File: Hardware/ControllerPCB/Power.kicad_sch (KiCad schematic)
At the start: 44 parts, among them Q1 NMOS_SO-8, U2 BTN9960LV, U3 BTN9960LV, U4 INA180A2, U6 TSR 0.5-2433

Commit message: Update PCB
Add solder jumper for +3.3V selection
fix DRC
aligne vias
export Gerber
add text
fix 3D Models
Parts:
- added JP6: SolderJumper_2_Open, Jumper:SolderJumper-2_P1.3mm_Open_TrianglePad1.0x1.5mm, symbol Jumper:SolderJumper_2_Open
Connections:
- net +3.3V: now also JP6.2 (B); no longer U6.3 (+VOUT)
- new net 3V3: JP6.1 (A), U6.3 (+VOUT)
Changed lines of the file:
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@@
   (junction (at 82.55 64.77) (diameter 0) (color 0 0 0 0)
   )
-  (junction (at 123.19 173.99) (diameter 0) (color 0 0 0 0)
+  (junction (at 129.54 173.99) (diameter 0) (color 0 0 0 0)
   )
   (junction (at 238.76 109.22) (diameter 0) (color 0 0 0 0)
@@
     (stroke (width 0) (type default))
   )
-  (wire (pts (xy 123.19 173.99) (xy 128.27 173.99))
+  (wire (pts (xy 129.54 173.99) (xy 134.62 173.99))
     (stroke (width 0) (type default))
   )
@@
     (stroke (width 0) (type default))
   )
-  (wire (pts (xy 119.38 173.99) (xy 123.19 173.99))
+  (wire (pts (xy 119.38 173.99) (xy 120.65 173.99))
     (stroke (width 0) (type default))
   )
@@
     (stroke (width 0) (type default))
   )
+  (wire (pts (xy 128.27 173.99) (xy 129.54 173.99))
+    (stroke (width 0) (type default))
+  )
   (wire (pts (xy 73.66 68.58) (xy 73.66 64.77))
     (stroke (width 0) (type default))
@@
     (stroke (width 0) (type default))
   )
-  (wire (pts (xy 123.19 170.18) (xy 123.19 173.99))
+  (wire (pts (xy 129.54 170.18) (xy 129.54 173.99))
     (stroke (width 0) (type default))
   )
@@
   (wire (pts (xy 77.47 31.75) (xy 77.47 33.02))
     (stroke (width 0) (type default))
+  )
+  (label "3V3" (at 119.38 173.99 0) (fields_autoplaced)
+    (effects (font (size 1.27 1.27)) (justify left bottom))
   )
   (label "+VBat*" (at 52.07 24.13 0) (fields_autoplaced)
@@
     (effects (font (size 1.27 1.27)) (justify right))
   )
-  (hierarchical_label "+3V3" (shape input) (at 128.27 173.99 0) (fields_autoplaced)
+  (hierarchical_label "+3V3" (shape input) (at 134.62 173.99 0) (fields_autoplaced)
     (effects (font (size 1.27 1.27)) (justify left))
   )
@@
     )
   )
-  (symbol (lib_id "power:+3.3V") (at 123.19 170.18 0) (unit 1)
+  (symbol (lib_id "power:+3.3V") (at 129.54 170.18 0) (unit 1)
     (in_bom yes) (on_board yes) (dnp no) (fields_autoplaced)
-    (property "Reference" "#PWR039" (at 123.19 173.99 0)
-      (effects (font (size 1.27 1.27)) hide)
-    )
-    (property "Value" "+3.3V" (at 123.19 165.1 0)
-      (effects (font (size 1.27 1.27)))
-    )
-    (property "Footprint" "" (at 123.19 170.18 0)
-      (effects (font (size 1.27 1.27)) hide)
-    )
-    (property "Datasheet" "" (at 123.19 170.18 0)
+    (property "Reference" "#PWR039" (at 129.54 173.99 0)
+      (effects (font (size 1.27 1.27)) hide)
+    )
+    (property "Value" "+3.3V" (at 129.54 165.1 0)
+      (effects (font (size 1.27 1.27)))
+    )
+    (property "Footprint" "" (at 129.54 170.18 0)
+      (effects (font (size 1.27 1.27)) hide)
+    )
+    (property "Datasheet" "" (at 129.54 170.18 0)
       (effects (font (size 1.27 1.27)) hide)
     )
@@
         )
       )
+    )
+  )
+  (symbol (lib_id "Jumper:SolderJumper_2_Open") (at 124.46 173.99 0) (unit 1)
+    (in_bom yes) (on_board yes) (dnp no)
+    (property "Reference" "JP6" (at 124.46 167.64 0)
+      (effects (font (size 1.27 1.27)))
+    )
+    (property "Value" "SolderJumper_2_Open" (at 124.46 177.8 0)
+      (effects (font (size 1.27 1.27)))
+    )
+    (property "Footprint" "Jumper:SolderJumper-2_P1.3mm_Open_TrianglePad1.0x1.5mm" (at 124.46 173.99 0)
+      (effects (font (size 1.27 1.27)) hide)
+    )
+    (property "Datasheet" "~" (at 124.46 173.99 0)
+      (effects (font (size 1.27 1.27)) hide)
+    )
+    (pin "1")
+    (pin "2")
+    (instances
+      (project "BugWiperPCB"
+        (path "/d31a15bd-db02-4d4c-9593-17c596d3182c/c3388659-287d-4904-b92a-4db1b844f22c"
+          (reference "JP6") (unit 1)
+        )
+      )

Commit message: update Controller PCB
Add additional capacitor
fix footprint Resistor Array CAT16
fix 3D Model CAT16
change traces from 0.5 to 0.4 mm
fix USB-C Footprint
Export Gerber
update BOM and Values
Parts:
- added C41: 1nF, Capacitor_SMD:C_0805_2012Metric_Pad1.18x1.45mm_HandSolder, symbol Device:C
- Q1: value NMOS_SO-8 -> SQJ146ELP-T1_GE3; Manufacturer_Name (none) -> Vishay; Manufacturer_Part_Number (none) -> SQJ146ELP-T1_GE3; Package (none) -> SO-8; Price (none) -> 1,00€
- U2, U3: Manufacturer_Name (none) -> infineon; Manufacturer_Part_Number (none) -> BTN9960LVAUMA1; Mouser Part Number (none) -> 726-BTN9960LVAUMA1; Price (none) -> 3,50€
- U4: Manufacturer_Name (none) -> texasinstruments; Manufacturer_Part_Number (none) -> INA180A2IDBVT; Mouser Part Number (none) -> 595-INA180A2IDBVT; Price (none) -> 0,85€
- U6: Alternative MF (none) -> RECOM; Alternative PN (none) -> R-78E3.3-0.5; Alternative Price (none) -> 2,5€; Manufacturer_Name (none) -> TRACO Power; Manufacturer_Part_Number (none) -> TSR 0.5-2433; Mouser Part Number (none) -> 495-TSR0.5-2433; Package (none) -> TO-220 compatible SIP3 package; Price (none) -> 6,44€
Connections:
- net 3V3: now also C41.2
- net at C26.2, L2.2, U6.1 (+VIN): now also C41.1
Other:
- moved on the sheet: JP6

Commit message: update BOM
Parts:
- C10, C7: value 100uF -> 22uF 25V; Manufacturer_Name (none) -> Samsung; Manufacturer_Part_Number (none) -> CL31A226KAHNNNE; Mouser Part Number (none) -> 187-CL31A226KAHNNNE; Mouser Price/Stock (none) -> 0,20€
- C11, C12, C13: Manufacturer_Name (none) -> KYOCERA AVX; Manufacturer_Part_Number (none) -> KAM15AR71H102KM; Mouser Part Number (none) -> 581-KAM15AR71H102KM; Mouser Price/Stock (none) -> 0,036€
- C14: value 10nF -> 10nF; Manufacturer_Name (none) -> Samsung; Manufacturer_Part_Number (none) -> CL10B103KB8NFNC; Mouser Part Number (none) -> 187-CL10B103KB8NFNC; Mouser Price/Stock (none) -> 0,016 €
- C15, C16, C17, C21, C23: value 25uF -> 22uF 25V; Manufacturer_Name (none) -> Samsung; Manufacturer_Part_Number (none) -> CL31A226KAHNNNE; Mouser Part Number (none) -> 187-CL31A226KAHNNNE; Mouser Price/Stock (none) -> 0,20€
- C18, C19, C20, C28: value 470uF -> 470uF 16V; Manufacturer_Name (none) -> Nichicon; Manufacturer_Part_Number (none) -> UWT1E331MNL1GS; Mouser Part Number (none) -> 647-UWT1E331MNL1S; Mouser Price/Stock (none) -> 0,256€
- C24, C25, C26: value 4.7uF -> 22uF 25V; Manufacturer_Name (none) -> Samsung; Manufacturer_Part_Number (none) -> CL31A226KAHNNNE; Mouser Part Number (none) -> 187-CL31A226KAHNNNE; Mouser Price/Stock (none) -> 0,20€
- C31: value 100nF -> 100nF; Manufacturer_Name (none) -> Samsung; Manufacturer_Part_Number (none) -> CL10B104KB8NNNC; Mouser Part Number (none) -> 187-CL10B104KB8NNNC; Mouser Price/Stock (none) -> 0,01 €
- C5, C9: value 100nF -> 1uF 50V; footprint Capacitor_SMD:C_0603_1608Metric -> Capacitor_SMD:C_0805_2012Metric; Manufacturer_Name (none) -> Samsung; Manufacturer_Part_Number (none) -> CL21B105MBFNNNE; Mouser Part Number (none) -> 187-CL21B105MBFNNNE; Mouser Price/Stock (none) -> 0,026€
- C6, C8, R7, R8: now left out of the parts list
- D2: value D_Zener -> D_Zener 10V; footprint Resistor_SMD:R_0805_2012Metric -> Diode_SMD:D_SOD-323_HandSoldering; Manufacturer_Name (none) -> Vishay; Manufacturer_Part_Number (none) -> GDZ10B-E3-08; Mouser Part Number (none) -> 78-GDZ10B-E3-08; Mouser Price/Stock (none) -> 0,143 €
- D3: value D_TVS -> D_TVS 15V
- L1: value IHLP4040DZER100M1A -> IHLP4040DZER100M11; Manufacturer_Name (none) -> Vishay; Manufacturer_Part_Number (none) -> IHLP4040DZER100M11; Mouser Part Number (none) -> 70-IHLP4040DZER100M1; Mouser Price/Stock (none) -> 1,18 €
- L2: Manufacturer_Name (none) -> Wurth Elektronik; Manufacturer_Part_Number (none) -> 74477410; Mouser Part Number (none) -> 710-74477410; Mouser Price/Stock (none) -> 1,61€
- Q1: Mouser Part Number (none) -> 78-SQJ146ELP-T1_GE3; Mouser Price/Stock (none) -> 1,02 €
- R10, R11: value 4k7 -> 10k
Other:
- moved on the sheet: C11, C12, C14, C16, C17, C18, C24, C25, C26, C28, C41, D2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

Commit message: update
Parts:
- D2: value D_Zener 10V -> GDZ10B-E3-08
- JP6: now left out of the parts list
- L2: value 10µH 2.2A -> 10uH 2.2A 74477410; JLCPCB Part # (none) -> C324269; JLCPCB Price (none) -> 0.1270; Nr 74477410 -> (none)
- R10, R11, R21, R38: Manufacturer_Name (none) -> YAGEO; Manufacturer_Part_Number (none) -> RC0603FR-1010KL; Mouser Part Number (none) -> 603-RC0603FR-1010KL; Mouser Price/Stock (none) -> 0,008 €
- R12, R9: Manufacturer_Name (none) -> YAGEO; Manufacturer_Part_Number (none) -> RC0603FR-071KL; Mouser Part Number (none) -> 603-RC0603FR-071KL; Mouser Price/Stock (none) -> 0,009 €
- R19: Manufacturer_Name (none) -> Bourns; Manufacturer_Part_Number (none) -> CR0603-FX-3301ELF; Mouser Part Number (none) -> 652-CR0603-FX3301ELF; Mouser Price/Stock (none) -> 0,009 €
- R20: Manufacturer_Name (none) -> YAGEO; Manufacturer_Part_Number (none) -> AC0603FR-1022KL; Mouser Part Number (none) -> 603-AC0603FR-1022KL; Mouser Price/Stock (none) -> 0,01 €
- R25: Manufacturer_Name (none) -> Welwyn Components / TT Electronics; Manufacturer_Part_Number (none) -> LRMAM1206-R004FT5; Mouser Part Number (none) -> 756-LRMAM1206R004FT5; Mouser Price/Stock (none) -> 0,57 €
- TH1: value Thermistor_NTC -> 10k NTC; Manufacturer_Name (none) -> Murata; Manufacturer_Part_Number (none) -> NCU18XH103E60RB; Mouser Part Number (none) -> 81-NCU18XH103E60RB; Mouser Price/Stock (none) -> 0,095 €
- U2, U3: Mouser Price/Stock (none) -> 2,40 €
- U4: JLCPCB Part # (none) -> C116203; JLCPCB Price (none) -> 0.2074; Mouser Price/Stock (none) -> 0,855€
- U6: Alternative MF RECOM -> TRACO Power; Alternative PN R-78E3.3-0.5 -> TSR 0.5-2433; Alternative Price 2,5€ -> 6,44 €; Manufacturer_Name TRACO Power -> RECOM; Manufacturer_Part_Number TSR 0.5-2433 -> R-78E3.3-0.5; Mouser Part Number 495-TSR0.5-2433 -> 919-R-78E3.3-0.5; Mouser Price/Stock (none) -> 2,75€; Package TO-220 compatible SIP3 package -> (none)

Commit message: update PCB and Gerber
change Switches to cheaper ones
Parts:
- C18, C19, C20, C28: value 470uF 16V -> 330uF 25V
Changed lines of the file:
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@@
       (effects (font (size 1.27 1.27)) (justify left))
     )
-    (property "Value" "470uF 16V" (at 66.04 74.93 0)
+    (property "Value" "330uF 25V" (at 66.04 74.93 0)
       (effects (font (size 1.27 1.27)) (justify left))
     )
@@
       (effects (font (size 1.27 1.27)) (justify left))
     )
-    (property "Value" "470uF 16V" (at 107.95 43.18 90)
+    (property "Value" "330uF 25V" (at 107.95 43.18 90)
       (effects (font (size 1.27 1.27)) (justify left))
     )
@@
       (effects (font (size 1.27 1.27)) (justify left))
     )
-    (property "Value" "470uF 16V" (at 74.93 74.93 0)
+    (property "Value" "330uF 25V" (at 74.93 74.93 0)
       (effects (font (size 1.27 1.27)) (justify left))
     )
@@
       (effects (font (size 1.27 1.27)) (justify left))
     )
-    (property "Value" "470uF 16V" (at 116.84 43.18 90)
-      (effects (font (size 1.27 1.27)) (justify left))
-    )
+    (property "Value" "330uF 25V" (at 116.84 43.18 90)
+      (effects (font (size 1.27 1.27)) (justify left))
+    )

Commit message: update BOM
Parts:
- C41: now left out of the parts list
- D3: value D_TVS 15V -> D_TVS 14V; Manufacturer_Name (none) -> Diodes Incorporated; Manufacturer_Part_Number (none) -> SMBJ14CA-13-F; Mouser Part Number (none) -> 621-SMBJ14CA-13-F; Mouser Price/Stock (none) -> 0,219 €
- Q1: Price 1,00€ -> (none)
- R7, R8: value 47k -> 22k; Manufacturer_Name (none) -> YAGEO; Manufacturer_Part_Number (none) -> AC0603FR-1022KL; Mouser Part Number (none) -> 603-AC0603FR-1022KL; Mouser Price/Stock (none) -> 0,01 €; now fitted; now in the parts list
- U2, U3: Price 3,50€ -> (none)
- U4: Price 0,85€ -> (none)
- U6: Price 6,44€ -> (none)
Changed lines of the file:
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@@
-      (effects (font (size 1.27 1.27)) hide)
-    )
-    (property "Price" "0,85€" (at 49.53 77.47 0)
       (effects (font (size 1.27 1.27)) hide)
     )
@@
     )
     (property "Mouser Part Number" "726-BTN9960LVAUMA1" (at 213.36 88.9 0)
-      (effects (font (size 1.27 1.27)) hide)
-    )
-    (property "Price" "3,50€" (at 213.36 88.9 0)
       (effects (font (size 1.27 1.27)) hide)
     )
@@
   )
   (symbol (lib_id "Device:R") (at 242.57 55.88 0) (unit 1)
-    (in_bom no) (on_board yes) (dnp yes) (fields_autoplaced)
+    (in_bom yes) (on_board yes) (dnp no) (fields_autoplaced)
     (property "Reference" "R7" (at 245.11 54.61 0)
       (effects (font (size 1.27 1.27)) (justify left))
     )
-    (property "Value" "47k" (at 245.11 57.15 0)
+    (property "Value" "22k" (at 245.11 57.15 0)
       (effects (font (size 1.27 1.27)) (justify left))
     )
@@
     )
     (property "JLCPCB Price" "" (at 242.57 55.88 0)
+      (effects (font (size 1.27 1.27)) hide)
+    )
+    (property "Manufacturer_Name" "YAGEO" (at 242.57 55.88 0)
+      (effects (font (size 1.27 1.27)) hide)
+    )
+    (property "Manufacturer_Part_Number" "AC0603FR-1022KL" (at 242.57 55.88 0)
+      (effects (font (size 1.27 1.27)) hide)
+    )
+    (property "Mouser Part Number" "603-AC0603FR-1022KL" (at 242.57 55.88 0)
+      (effects (font (size 1.27 1.27)) hide)
+    )
+    (property "Mouser Price/Stock" "0,01 €" (at 242.57 55.88 0)
       (effects (font (size 1.27 1.27)) hide)
     )
@@
       (effects (font (size 1.27 1.27)) (justify right))
     )
-    (property "Value" "D_TVS 15V" (at 62.23 27.94 0)
+    (property "Value" "D_TVS 14V" (at 62.23 27.94 0)
       (effects (font (size 1.27 1.27)) (justify right))
     )
@@
       (effects (font (size 1.27 1.27)) hide)
     )
+    (property "Manufacturer_Name" "Diodes Incorporated" (at 59.69 31.75 0)
+      (effects (font (size 1.27 1.27)) hide)
+    )
+    (property "Manufacturer_Part_Number" "SMBJ14CA-13-F" (at 59.69 31.75 0)
+      (effects (font (size 1.27 1.27)) hide)
+    )
+    (property "Mouser Part Number" "621-SMBJ14CA-13-F" (at 59.69 31.75 0)
+      (effects (font (size 1.27 1.27)) hide)
+    )
+    (property "Mouser Price/Stock" "0,219 €" (at 59.69 31.75 0)
+      (effects (font (size 1.27 1.27)) hide)
+    )
     (pin "2")
     (pin "1")
@@
   )
   (symbol (lib_id "Device:R") (at 242.57 105.41 0) (unit 1)
-    (in_bom no) (on_board yes) (dnp yes) (fields_autoplaced)
+    (in_bom yes) (on_board yes) (dnp no) (fields_autoplaced)
     (property "Reference" "R8" (at 245.11 104.14 0)
       (effects (font (size 1.27 1.27)) (justify left))
     )
-    (property "Value" "47k" (at 245.11 106.68 0)
+    (property "Value" "22k" (at 245.11 106.68 0)
       (effects (font (size 1.27 1.27)) (justify left))
     )
@@
     )
     (property "JLCPCB Price" "" (at 242.57 105.41 0)
+      (effects (font (size 1.27 1.27)) hide)
+    )
+    (property "Manufacturer_Name" "YAGEO" (at 242.57 105.41 0)
+      (effects (font (size 1.27 1.27)) hide)
+    )
+    (property "Manufacturer_Part_Number" "AC0603FR-1022KL" (at 242.57 105.41 0)
+      (effects (font (size 1.27 1.27)) hide)
+    )
+    (property "Mouser Part Number" "603-AC0603FR-1022KL" (at 242.57 105.41 0)
+      (effects (font (size 1.27 1.27)) hide)
+    )
+    (property "Mouser Price/Stock" "0,01 €" (at 242.57 105.41 0)
       (effects (font (size 1.27 1.27)) hide)
     )
@@
   )
   (symbol (lib_id "Device:C") (at 92.71 133.35 90) (unit 1)
-    (in_bom yes) (on_board yes) (dnp yes)
+    (in_bom no) (on_board yes) (dnp yes)
     (property "Reference" "C41" (at 93.98 127 90)
       (effects (font (size 1.27 1.27)) (justify left))
@@
     )
     (property "Mouser Part Number" "726-BTN9960LVAUMA1" (at 213.36 39.37 0)
-      (effects (font (size 1.27 1.27)) hide)
-    )
-    (property "Price" "3,50€" (at 213.36 39.37 0)
       (effects (font (size 1.27 1.27)) hide)
     )
@@
       (effects (font (size 1.27 1.27)) hide)
     )
-    (property "Price" "6,44€" (at 72.39 147.32 0)
-      (effects (font (size 1.27 1.27)) hide)
-    )
     (property "Mouser Price/Stock" "2,75€" (at 72.39 147.32 0)
       (effects (font (size 1.27 1.27)) hide)
@@
       (effects (font (size 1.27 1.27)) hide)
     )
-    (property "Price" "1,00€" (at 68.58 26.67 0)
-      (effects (font (size 1.27 1.27)) hide)
-    )
     (property "Alternative MF" "" (at 68.58 26.67 0)
       (effects (font (size 1.27 1.27)) hide)
@@
       (effects (font (size 1.27 1.27)) hide)
     )
-    (property "Nr" "" (at 62.23 147.32 0)
-      (effects (font (size 1.27 1.27)) hide)
-    )

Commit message: update PCB to view Values and Refs
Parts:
- C10, C15, C16, C17, C21, C23, C24, C25, C26, C7: value 22uF 25V -> 22uF
- C14: value 10nF -> 10nF
- C18, C19, C20, C28: value 330uF 25V -> 330uF
- C31: value 100nF -> 100nF
- C5, C9: value 1uF 50V -> 1uF
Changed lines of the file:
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@@
       (effects (font (size 1.27 1.27)) (justify left))
     )
-    (property "Value" "22uF 25V" (at 90.17 41.91 90)
+    (property "Value" "22uF" (at 90.17 41.91 90)
       (effects (font (size 1.27 1.27)) (justify left))
     )
@@
       (effects (font (size 1.27 1.27)) (justify left))
     )
-    (property "Value" "22uF 25V" (at 45.72 151.13 90)
+    (property "Value" "22uF" (at 45.72 151.13 90)
       (effects (font (size 1.27 1.27)) (justify left))
     )
@@
       (effects (font (size 1.27 1.27)) (justify left))
     )
-    (property "Value" "22uF 25V" (at 68.58 151.13 90)
+    (property "Value" "22uF" (at 68.58 151.13 90)
       (effects (font (size 1.27 1.27)) (justify left))
     )
@@
       (effects (font (size 1.27 1.27)) (justify left))
     )
-    (property "Value" "22uF 25V" (at 33.02 151.13 90)
+    (property "Value" "22uF" (at 33.02 151.13 90)
       (effects (font (size 1.27 1.27)) (justify left))
     )
@@
       (effects (font (size 1.27 1.27)) (justify left))
     )
-    (property "Value" "22uF 25V" (at 54.61 27.94 90)
+    (property "Value" "22uF" (at 54.61 27.94 90)
       (effects (font (size 1.27 1.27)) (justify left))
     )
@@
       (effects (font (size 1.27 1.27)) (justify left))
     )
-    (property "Value" "330uF 25V" (at 66.04 74.93 0)
+    (property "Value" "330uF" (at 66.04 74.93 0)
       (effects (font (size 1.27 1.27)) (justify left))
     )
@@
       (effects (font (size 1.27 1.27)) (justify left))
     )
-    (property "Value" "1uF 50V" (at 255.27 57.15 0)
+    (property "Value" "1uF" (at 255.27 57.15 0)
       (effects (font (size 1.27 1.27)) (justify left))
     )
@@
       (effects (font (size 1.27 1.27)) (justify left))
     )
-    (property "Value" "22uF 25V" (at 269.24 106.68 0)
+    (property "Value" "22uF" (at 269.24 106.68 0)
       (effects (font (size 1.27 1.27)) (justify left))
     )
@@
       (effects (font (size 1.27 1.27)) (justify left))
     )
-    (property "Value" "330uF 25V" (at 107.95 43.18 90)
+    (property "Value" "330uF" (at 107.95 43.18 90)
       (effects (font (size 1.27 1.27)) (justify left))
     )
@@
       (effects (font (size 1.27 1.27)) (justify left))
     )
-    (property "Value" "22uF 25V" (at 33.02 35.56 90)
+    (property "Value" "22uF" (at 33.02 35.56 90)
       (effects (font (size 1.27 1.27)) (justify left))
     )
@@
       (effects (font (size 1.27 1.27)) (justify left))
     )
-    (property "Value" "330uF 25V" (at 74.93 74.93 0)
+    (property "Value" "330uF" (at 74.93 74.93 0)
       (effects (font (size 1.27 1.27)) (justify left))
     )
@@
       (effects (font (size 1.27 1.27)) (justify left))
     )
-    (property "Value" "22uF 25V" (at 83.82 74.93 0)
+    (property "Value" "22uF" (at 83.82 74.93 0)
       (effects (font (size 1.27 1.27)) (justify left))
     )
@@
       (effects (font (size 1.27 1.27)) (justify left))
     )
-    (property "Value" "330uF 25V" (at 116.84 43.18 90)
+    (property "Value" "330uF" (at 116.84 43.18 90)
       (effects (font (size 1.27 1.27)) (justify left))
     )
@@
       (effects (font (size 1.27 1.27)) (justify left))
     )
-    (property "Value" "22uF 25V" (at 99.06 41.91 90)
+    (property "Value" "22uF" (at 99.06 41.91 90)
       (effects (font (size 1.27 1.27)) (justify left))
     )
@@
       (effects (font (size 1.27 1.27)) (justify left))
     )
-    (property "Value" "100nF " (at 212.09 144.78 0)
+    (property "Value" "100nF" (at 212.09 144.78 0)
       (effects (font (size 1.27 1.27)) (justify left))
     )
@@
       (effects (font (size 1.27 1.27)) (justify left))
     )
-    (property "Value" "22uF 25V" (at 269.24 57.15 0)
+    (property "Value" "22uF" (at 269.24 57.15 0)
       (effects (font (size 1.27 1.27)) (justify left))
     )
@@
       (effects (font (size 1.27 1.27)) (justify left))
     )
-    (property "Value" "1uF 50V" (at 255.27 106.68 0)
+    (property "Value" "1uF" (at 255.27 106.68 0)
       (effects (font (size 1.27 1.27)) (justify left))
     )
@@
       (effects (font (size 1.27 1.27)) (justify left))
     )
-    (property "Value" "10nF " (at 72.39 43.18 0)
-      (effects (font (size 1.27 1.27)) (justify left))
-    )
+    (property "Value" "10nF" (at 72.39 43.18 0)
+      (effects (font (size 1.27 1.27)) (justify left))
+    )

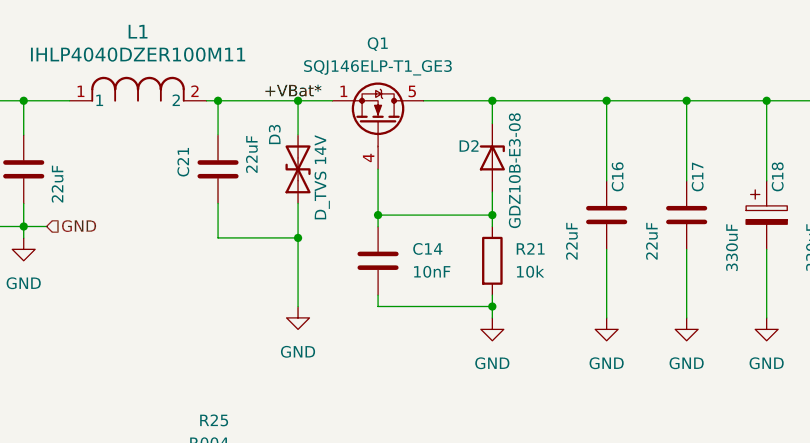
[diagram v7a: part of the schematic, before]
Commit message: update Controller PCB PDF Export and layer of Values and Reference
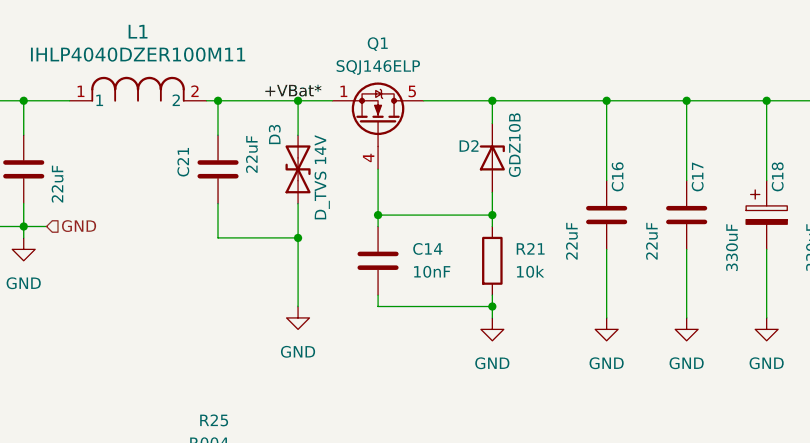
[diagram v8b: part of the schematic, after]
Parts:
- D2: value GDZ10B-E3-08 -> GDZ10B
- Q1: value SQJ146ELP-T1_GE3 -> SQJ146ELP
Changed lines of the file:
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@@
       (effects (font (size 1.27 1.27)) (justify left))
     )
-    (property "Value" "GDZ10B-E3-08" (at 83.82 25.4 0)
+    (property "Value" "GDZ10B" (at 83.82 25.4 0)
       (effects (font (size 1.27 1.27)) (justify left))
     )
@@
       (effects (font (size 1.27 1.27)))
     )
-    (property "Value" "SQJ146ELP-T1_GE3" (at 68.58 20.32 90)
-      (effects (font (size 1.27 1.27)))
-    )
+    (property "Value" "SQJ146ELP" (at 68.58 20.32 90)
+      (effects (font (size 1.27 1.27)))
+    )
